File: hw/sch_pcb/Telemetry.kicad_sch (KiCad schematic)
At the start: 41 parts, among them J1 HEADER_2x01_PARALLEL, J10 HEADER_2x01_PARALLEL, J2 HEADER_2x01_PARALLEL, J3 HEADER_2x01_PARALLEL, J4 HEADER_2x01_PARALLEL, J5 HEADER_2x01_PARALLEL, J6 HEADER_2x01_PARALLEL, J7 MCX, J8 HEADER_2x01_PARALLEL, J9 HEADER_2x01_PARALLEL, U1 SX1262, U2 PE4259, Y1 32MHz

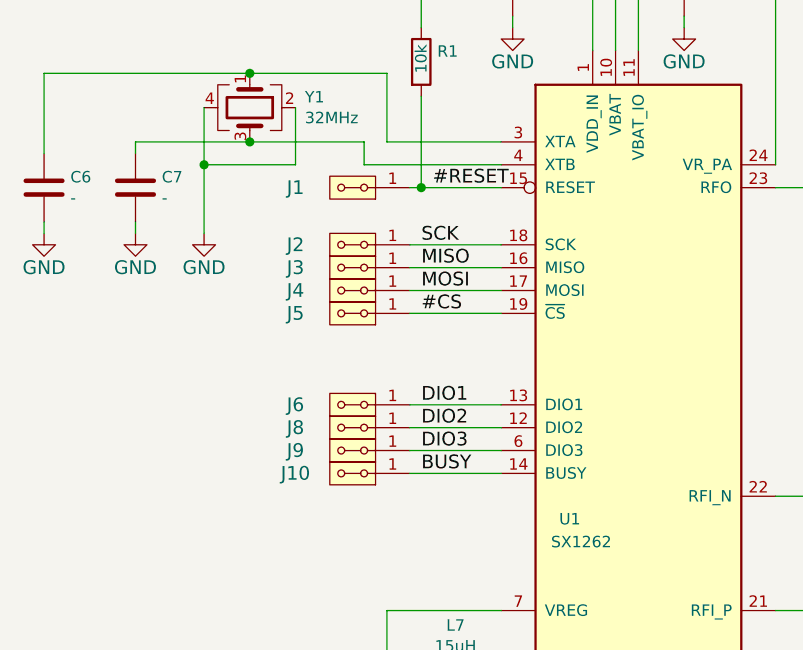
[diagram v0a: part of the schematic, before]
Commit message: schematics update
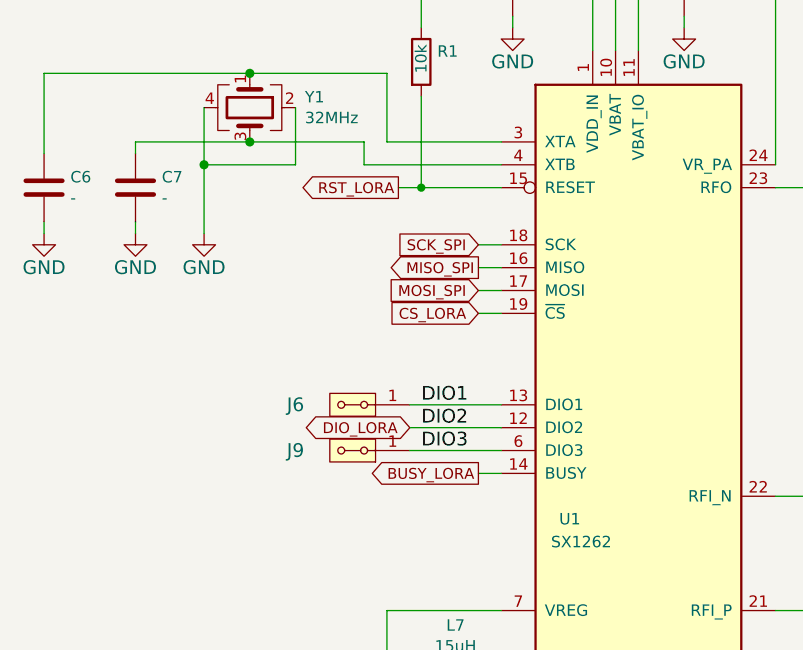
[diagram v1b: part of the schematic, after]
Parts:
- removed J1, J10, J2, J3, J4, J5, J8: HEADER_2x01_PARALLEL, Mlab_Pin_Headers:Straight_2x01, symbol ISM02A-rescue:HEADER_2x01_PARALLEL-MLAB_HEADER
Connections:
- net #CS renamed CS_LORA
- net #RESET renamed RST_LORA
- net BUSY renamed BUSY_LORA
- net DIO2 renamed DIO_LORA
- net MISO renamed MISO_SPI
- net MOSI renamed MOSI_SPI
- net SCK renamed SCK_SPI

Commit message: progress?
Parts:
- removed J6, J9: HEADER_2x01_PARALLEL, Mlab_Pin_Headers:Straight_2x01, symbol ISM02A-rescue:HEADER_2x01_PARALLEL-MLAB_HEADER
- added J13: HEADER_2x02_PARALLEL, Mlab_Pin_Headers:Straight_2x02, symbol MLAB_HEADER:HEADER_2x02_PARALLEL
- C41: renamed from C6; footprint Capacitor_SMD:C_0603_1608Metric_Pad1.05x0.95mm_HandSolder -> Mlab_C:SMD-0805
- C42: renamed from C7; footprint Capacitor_SMD:C_0603_1608Metric_Pad1.05x0.95mm_HandSolder -> Mlab_C:SMD-0805
- C43: renamed from C19; footprint Capacitor_SMD:C_0603_1608Metric_Pad1.05x0.95mm_HandSolder -> Mlab_C:SMD-0805
- C44: renamed from C1; footprint Capacitor_SMD:C_0603_1608Metric_Pad1.05x0.95mm_HandSolder -> Mlab_C:SMD-0805
- C45: renamed from C2; footprint Capacitor_SMD:C_0603_1608Metric_Pad1.05x0.95mm_HandSolder -> Mlab_C:SMD-0805
- C46: renamed from C3; footprint Capacitor_SMD:C_0603_1608Metric_Pad1.05x0.95mm_HandSolder -> Mlab_C:SMD-0805
- C47: renamed from C17; footprint Capacitor_SMD:C_0603_1608Metric_Pad1.05x0.95mm_HandSolder -> Mlab_C:SMD-0805
- C48: renamed from C4; footprint Capacitor_SMD:C_0603_1608Metric_Pad1.05x0.95mm_HandSolder -> Mlab_C:SMD-0805
- C49: renamed from C15; footprint Capacitor_SMD:C_0603_1608Metric_Pad1.05x0.95mm_HandSolder -> Mlab_C:SMD-0805
- C50: renamed from C9; footprint Capacitor_SMD:C_0603_1608Metric_Pad1.05x0.95mm_HandSolder -> Mlab_C:SMD-0805
- C51: renamed from C16; footprint Capacitor_SMD:C_0603_1608Metric_Pad1.05x0.95mm_HandSolder -> Mlab_C:SMD-0805
- C52: renamed from C5; footprint Capacitor_SMD:C_0603_1608Metric_Pad1.05x0.95mm_HandSolder -> Mlab_C:SMD-0805
- C53: renamed from C10; footprint Capacitor_SMD:C_0603_1608Metric_Pad1.05x0.95mm_HandSolder -> Mlab_C:SMD-0805
- C54: renamed from C8; footprint Capacitor_SMD:C_0603_1608Metric_Pad1.05x0.95mm_HandSolder -> Mlab_C:SMD-0805
- C55: renamed from C11; footprint Capacitor_SMD:C_0603_1608Metric_Pad1.05x0.95mm_HandSolder -> Mlab_C:SMD-0805
- C56: renamed from C18; footprint Capacitor_SMD:C_0603_1608Metric_Pad1.05x0.95mm_HandSolder -> Mlab_C:SMD-0805
- C57: renamed from C12; footprint Capacitor_SMD:C_0603_1608Metric_Pad1.05x0.95mm_HandSolder -> Mlab_C:SMD-0805
- C58: renamed from C13; footprint Capacitor_SMD:C_0603_1608Metric_Pad1.05x0.95mm_HandSolder -> Mlab_C:SMD-0805
- C59: renamed from C14; footprint Capacitor_SMD:C_0603_1608Metric_Pad1.05x0.95mm_HandSolder -> Mlab_C:SMD-0805
- L5: renamed from L7; footprint Mlab_R:SMD-0805 -> Inductor_SMD:L_0402_1005Metric
- R46: renamed from R1; footprint Mlab_R:SMD-0603 -> Mlab_R:SMD-0805
- R47: renamed from R2; footprint Mlab_R:SMD-0603 -> Mlab_R:SMD-0805
- renumbered J7 to J23, L4 to L10, L5 to L11, L2 to L7, L1 to L8, L3 to L9, U1 to U11, U2 to U12, Y1 to Y3
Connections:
- net DIO1: now also J13.3, J13.4
- net DIO3: now also J13.1, J13.2
- net +3V3 renamed +3.3V

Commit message: silkmasks done
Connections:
- net DIO1: now also J13.1, J13.2; no longer J13.3, J13.4
- net DIO3: now also J13.3, J13.4; no longer J13.1, J13.2
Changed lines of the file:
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@@
-	(wire
-		(pts
-			(xy 52.07 107.95) (xy 52.07 106.68)
-		)
-		(stroke
-			(width 0)
-			(type solid)
-		)
-	)
 	(wire
 		(pts
@@
 	(wire
 		(pts
+			(xy 74.93 107.95) (xy 83.82 107.95)
+		)
+		(stroke
+			(width 0)
+			(type default)
+		)
+	)
+	(wire
+		(pts
 			(xy 214.63 93.98) (xy 214.63 113.03)
 		)
@@
 	(wire
 		(pts
-			(xy 52.07 104.14) (xy 52.07 102.87)
-		)
-		(stroke
-			(width 0)
-			(type default)
-		)
-	)
-	(wire
-		(pts
 			(xy 55.88 66.04) (xy 71.12 66.04)
 		)
@@
 	(wire
 		(pts
+			(xy 74.93 102.87) (xy 83.82 102.87)
+		)
+		(stroke
+			(width 0)
+			(type default)
+		)
+	)
+	(wire
+		(pts
 			(xy 114.3 125.73) (xy 121.92 125.73)
 		)
@@
 	(wire
 		(pts
-			(xy 52.07 107.95) (xy 83.82 107.95)
-		)
-		(stroke
-			(width 0)
-			(type solid)
-		)
-	)
-	(wire
-		(pts
 			(xy 43.18 73.66) (xy 43.18 74.93)
 		)
@@
 		)
 	)
-	(wire
-		(pts
-			(xy 52.07 102.87) (xy 83.82 102.87)
-		)
-		(stroke
-			(width 0)
-			(type default)
+	(label "DIO1"
+		(at 52.07 106.68 0)
+		(fields_autoplaced yes)
+		(effects
+			(font
+				(size 1.524 1.524)
+			)
+			(justify left bottom)
 		)
 	)
@@
 		)
 	)
+	(label "DIO3"
+		(at 52.07 104.14 0)
+		(fields_autoplaced yes)
+		(effects
+			(font
+				(size 1.524 1.524)
+			)
+			(justify left bottom)
+		)
+	)
 	(label "DIO2"
 		(at 233.68 127 0)
@@
 	)
 	(label "DIO3"
-		(at 52.07 107.95 0)
+		(at 74.93 107.95 0)
 		(fields_autoplaced yes)
 		(effects
@@
 	)
 	(label "DIO1"
-		(at 52.07 102.87 0)
+		(at 74.93 102.87 0)
 		(fields_autoplaced yes)
 		(effects

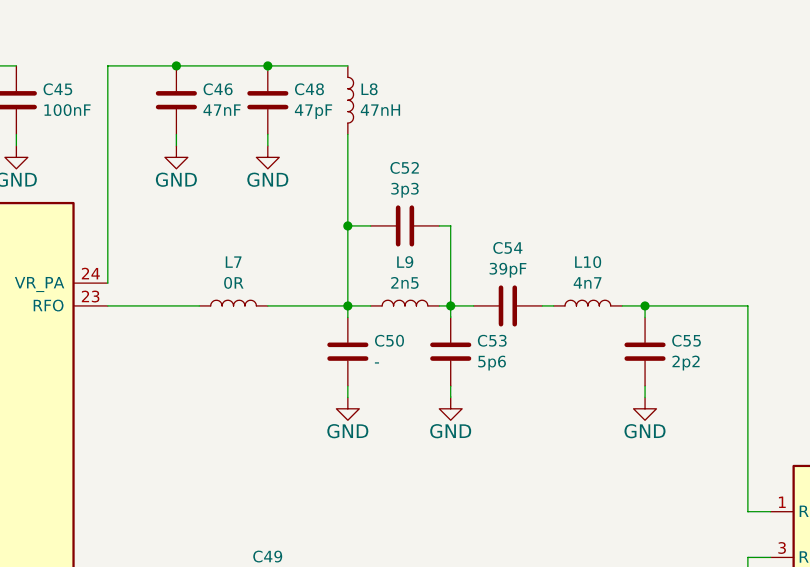
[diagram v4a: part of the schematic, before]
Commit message: Update footprints. Improve layout Fix some DRC errors. Set components values matching inventory.
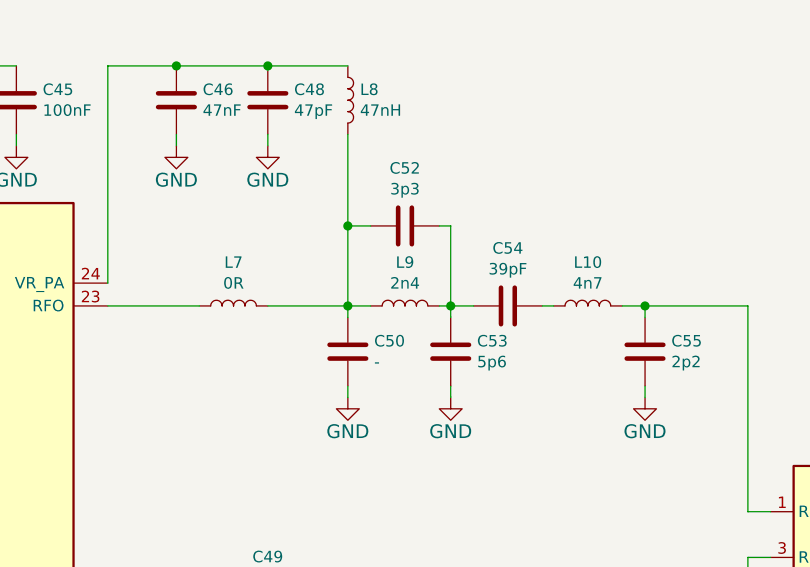
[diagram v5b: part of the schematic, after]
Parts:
- C41, C42, C43, C44, C45, C46, C47, C48, C56: footprint Mlab_C:SMD-0805 -> Capacitor_SMD:C_0805_2012Metric
- C49, C50, C51, C52, C53, C54, C55, C57, C58, C59: footprint Mlab_C:SMD-0805 -> Capacitor_SMD:C_0603_1608Metric
- L10: footprint Inductor_SMD:L_0402_1005Metric -> Inductor_SMD:L_0603_1608Metric; UST_ID 5dad574f128750448eca1986 -> 671226edd509c19f2ce8ed2d
- L11, L6, L7, L8: footprint Inductor_SMD:L_0402_1005Metric -> Inductor_SMD:L_0603_1608Metric
- L5: footprint Inductor_SMD:L_0402_1005Metric -> Inductor_SMD:L_0805_2012Metric
- L9: value 2n5 -> 2n4; footprint Inductor_SMD:L_0402_1005Metric -> Inductor_SMD:L_0603_1608Metric
- R46, R47: footprint Mlab_R:SMD-0805 -> Resistor_SMD:R_0805_2012Metric
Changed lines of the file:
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@@
 			)
 		)
-		(property "Footprint" "Mlab_R:SMD-0805"
+		(property "Footprint" "Resistor_SMD:R_0805_2012Metric"
 			(at 73.152 64.77 90)
 			(effects
@@
 		(on_board yes)
 		(dnp no)
+		(fields_autoplaced yes)
 		(property "Reference" "L11"
 			(at 237.49 99.314 90)
@@
 			)
 		)
-		(property "Footprint" "Inductor_SMD:L_0402_1005Metric"
+		(property "Footprint" "Inductor_SMD:L_0603_1608Metric"
 			(at 237.49 104.14 0)
 			(effects
@@
 			)
 		)
-		(property "Footprint" "Inductor_SMD:L_0402_1005Metric"
+		(property "Footprint" "Inductor_SMD:L_0603_1608Metric"
 			(at 140.97 55.88 0)
 			(effects
@@
 		(on_board yes)
 		(dnp no)
+		(fields_autoplaced yes)
 		(property "Reference" "#PWR0156"
 			(at 245.11 120.65 0)
@@
 			)
 		)
-		(property "Footprint" "Mlab_C:SMD-0805"
+		(property "Footprint" "Capacitor_SMD:C_0603_1608Metric"
 			(at 153.3652 87.63 0)
 			(effects
@@
 			)
 		)
-		(property "Footprint" "Mlab_C:SMD-0805"
+		(property "Footprint" "Capacitor_SMD:C_0805_2012Metric"
 			(at 33.9852 82.55 0)
 			(effects
@@
 			)
 		)
-		(property "Footprint" "Mlab_C:SMD-0805"
+		(property "Footprint" "Capacitor_SMD:C_0805_2012Metric"
 			(at 44.1452 82.55 0)
 			(effects
@@
 			)
 		)
-		(property "Footprint" "Mlab_C:SMD-0805"
+		(property "Footprint" "Capacitor_SMD:C_0603_1608Metric"
 			(at 141.9352 87.63 0)
 			(effects
@@
 			)
 		)
+		(property "UST_ID" ""
+			(at 140.97 83.82 0)
+			(effects
+				(font
+					(size 1.27 1.27)
+				)
+				(hide yes)
+			)
+		)
 		(pin "1"
 		)
@@
 			)
 		)
-		(property "Footprint" "Inductor_SMD:L_0402_1005Metric"
+		(property "Footprint" "Inductor_SMD:L_0603_1608Metric"
 			(at 167.64 78.74 0)
 			(effects
@@
 			)
 		)
-		(property "UST_ID" "5dad574f128750448eca1986"
+		(property "UST_ID" "671226edd509c19f2ce8ed2d"
 			(at 265.43 262.89 0)
 			(effects
@@
 			)
 		)
-		(property "Footprint" "Mlab_C:SMD-0805"
+		(property "Footprint" "Capacitor_SMD:C_0603_1608Metric"
 			(at 174.9552 87.63 0)
 			(effects
@@
 			)
 		)
-		(property "Footprint" "Mlab_C:SMD-0805"
+		(property "Footprint" "Capacitor_SMD:C_0603_1608Metric"
 			(at 143.51 70.8152 0)
 			(effects
@@
 			)
 		)
-		(property "Footprint" "Mlab_C:SMD-0805"
+		(property "Footprint" "Capacitor_SMD:C_0805_2012Metric"
 			(at 122.8852 59.69 0)
 			(effects
@@
 			)
 		)
-		(property "Footprint" "Mlab_C:SMD-0805"
+		(property "Footprint" "Capacitor_SMD:C_0603_1608Metric"
 			(at 154.94 79.7052 0)
 			(effects
@@
 			)
 		)
-		(property "Footprint" "Mlab_C:SMD-0805"
+		(property "Footprint" "Capacitor_SMD:C_0805_2012Metric"
 			(at 219.4052 135.89 0)
 			(effects
@@
 			)
 		)
-		(property "Footprint" "Inductor_SMD:L_0402_1005Metric"
+		(property "Footprint" "Inductor_SMD:L_0603_1608Metric"
 			(at 128.27 78.74 0)
 			(effects
@@
 		(on_board yes)
 		(dnp no)
+		(fields_autoplaced yes)
 		(property "Reference" "C58"
 			(at 232.791 108.0516 0)
@@
 			)
 		)
-		(property "Footprint" "Mlab_C:SMD-0805"
+		(property "Footprint" "Capacitor_SMD:C_0603_1608Metric"
 			(at 228.9048 105.41 0)
 			(effects
@@
 			)
 		)
-		(property "Footprint" "Mlab_C:SMD-0805"
+		(property "Footprint" "Capacitor_SMD:C_0805_2012Metric"
 			(at 86.0552 59.69 0)
 			(effects
@@
 			)
 		)
-		(property "Footprint" "Mlab_C:SMD-0805"
+		(property "Footprint" "Capacitor_SMD:C_0805_2012Metric"
 			(at 122.8852 134.62 0)
 			(effects
@@
 			)
 		)
-		(property "Footprint" "Inductor_SMD:L_0402_1005Metric"
+		(property "Footprint" "Inductor_SMD:L_0805_2012Metric"
 			(at 78.74 132.08 0)
 			(effects
@@
 			)
 		)
-		(property "Value" "2n5"
+		(property "Value" "2n4"
 			(at 147.32 76.2254 90)
 			(effects
@@
 			)
 		)
-		(property "Footprint" "Inductor_SMD:L_0402_1005Metric"
+		(property "Footprint" "Inductor_SMD:L_0603_1608Metric"
 			(at 147.32 78.74 0)
 			(effects
@@
 			)
 		)
-		(property "Footprint" "Mlab_C:SMD-0805"
+		(property "Footprint" "Capacitor_SMD:C_0805_2012Metric"
 			(at 133.0452 59.69 0)
 			(effects
@@
 			)
 		)
-		(property "Footprint" "Mlab_C:SMD-0805"
+		(property "Footprint" "Capacitor_SMD:C_0603_1608Metric"
 			(at 128.27 113.9952 0)
 			(effects
@@
 			)
 		)
-		(property "Footprint" "Mlab_R:SMD-0805"
+		(property "Footprint" "Resistor_SMD:R_0805_2012Metric"
 			(at 228.6 128.778 90)
 			(effects
@@
 			)
 		)
-		(property "Footprint" "Mlab_C:SMD-0805"
+		(property "Footprint" "Capacitor_SMD:C_0805_2012Metric"
 			(at 105.1052 59.69 0)
 			(effects
@@
 		(on_board yes)
 		(dnp no)
+		(fields_autoplaced yes)
 		(property "Reference" "C59"
 			(at 248.031 108.0516 0)
@@
 			)
 		)
-		(property "Footprint" "Mlab_C:SMD-0805"
+		(property "Footprint" "Capacitor_SMD:C_0603_1608Metric"
 			(at 244.1448 105.41 0)
 			(effects
@@
 			)
 		)
-		(property "Footprint" "Mlab_C:SMD-0805"
+		(property "Footprint" "Capacitor_SMD:C_0603_1608Metric"
 			(at 141.9352 123.19 0)
 			(effects
@@
 			)
 		)
+		(property "UST_ID" ""
+			(at 140.97 119.38 0)
+			(effects
+				(font
+					(size 1.27 1.27)
+				)
+				(hide yes)
+			)
+		)
 		(pin "1"
 		)
@@
 			)
 		)
-		(property "Footprint" "Inductor_SMD:L_0402_1005Metric"
+		(property "Footprint" "Inductor_SMD:L_0603_1608Metric"
 			(at 121.92 119.38 0)
 			(effects
@@
 			)
 		)
-		(property "Footprint" "Mlab_C:SMD-0805"
+		(property "Footprint" "Capacitor_SMD:C_0805_2012Metric"
 			(at 72.0852 142.24 0)
 			(effects
@@
 		(on_board yes)
 		(dnp no)
+		(fields_autoplaced yes)
 		(property "Reference" "C57"
 			(at 222.25 97.7392 90)
@@
 			)
 		)
-		(property "Footprint" "Mlab_C:SMD-0805"
+		(property "Footprint" "Capacitor_SMD:C_0603_1608Metric"
 			(at 218.44 105.1052 0)
 			(effects
@@
 		(on_board yes)
 		(dnp no)
+		(fields_autoplaced yes)
 		(property "Reference" "#PWR0155"
 			(at 229.87 120.65 0)

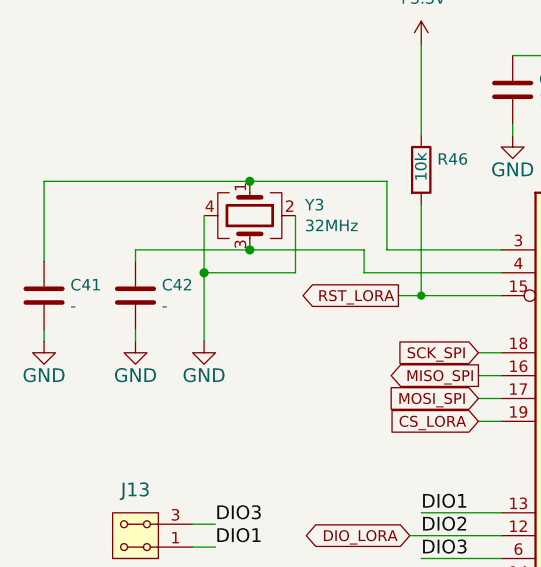
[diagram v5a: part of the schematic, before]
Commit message: Fix component placement and layout of telemetry transceiver.
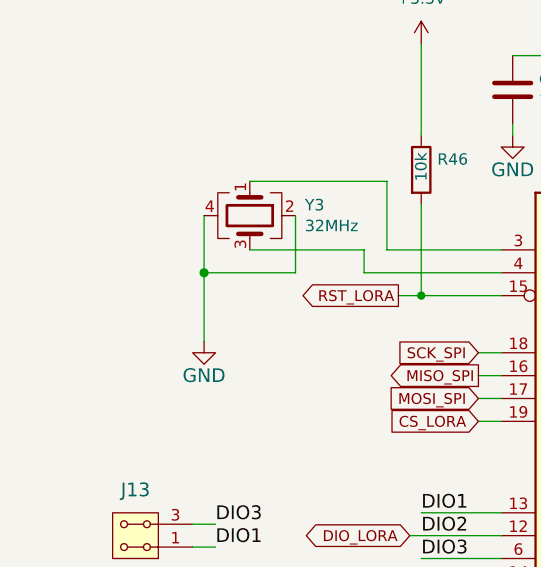
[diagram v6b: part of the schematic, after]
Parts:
- removed C41, C42: -, Capacitor_SMD:C_0805_2012Metric, symbol ISM02A-rescue:C-Device-ISM02A-rescue
- C47: footprint Capacitor_SMD:C_0805_2012Metric -> Capacitor_SMD:C_0603_1608Metric
